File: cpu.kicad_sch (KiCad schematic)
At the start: 22 parts, among them IC1 68HC000, IC2 LHP6323, IC7 MSM54C864

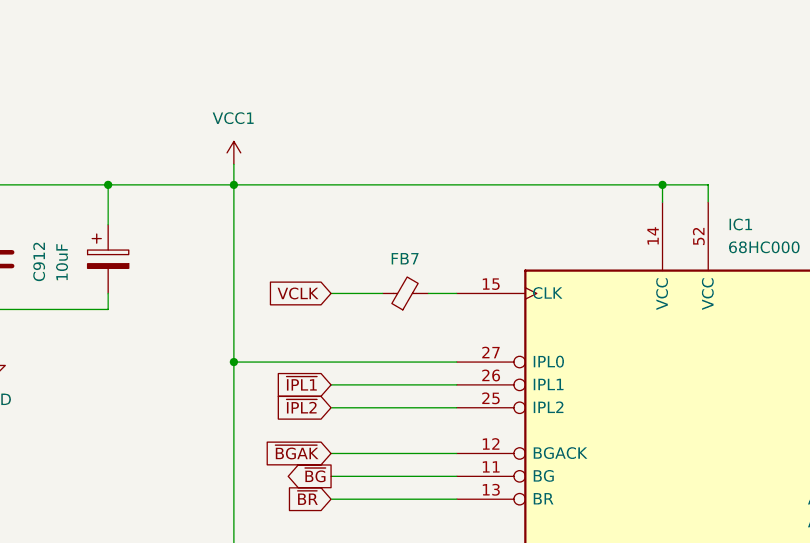
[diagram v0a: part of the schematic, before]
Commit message: Ferrite Bead LCSC Part update
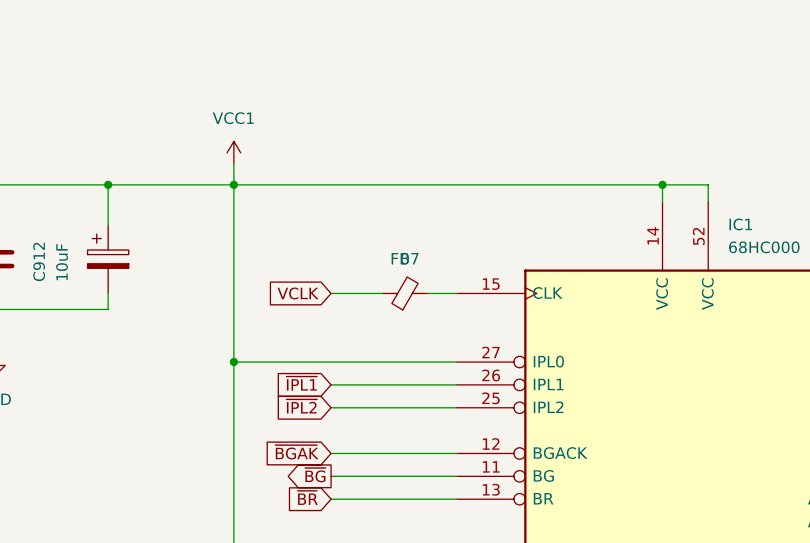
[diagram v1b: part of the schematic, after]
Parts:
- FB7: value ~ -> 0; LCSC Part # C2441367 -> C91037
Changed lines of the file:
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@@
       (effects (font (size 1.27 1.27)))
     )
-    (property "Value" "~" (at 135.2169 55.88 90)
+    (property "Value" "0" (at 135.2169 55.88 90)
       (effects (font (size 1.27 1.27)))
     )
@@
       (effects (font (size 1.27 1.27)) hide)
     )
-    (property "LCSC Part #" "C2441367" (at 135.255 59.69 0)
+    (property "LCSC Part #" "C91037" (at 135.255 59.69 0)
       (effects (font (size 1.27 1.27)) hide)
     )

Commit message: more component parts updated
Full in the * as PAL versions.
Added MPN for PCBWAY
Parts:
- C16, C18, C3, C5: MPN (none) -> VJ0805A101FXJPW1BC
- C17, C2: MPN (none) -> VJ0805A330FXJPW1BC
- C903: MPN (none) -> VJ0805Y223JXJPW1BC
- C903: MPN (none) -> VJ0805Y104JXJMT
- CA601, CA602, CA603, CA604: MPN (none) -> CA0612KRNPO9BN330
- FB7: MPN (none) -> CBG201209U000T
- R3: MPN (none) -> CRCW0805220RFKEAC
- R3: MPN (none) -> CRCW0805150RFKEAHP
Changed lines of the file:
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@@
+      (effects (font (size 1.27 1.27)) hide)
+    )
+    (property "MPN" "CA0612KRNPO9BN330" (at 140.97 231.14 0)
       (effects (font (size 1.27 1.27)) hide)
     )
@@
       (effects (font (size 1.27 1.27)) hide)
     )
+    (property "MPN" "VJ0805Y223JXJPW1BC" (at 323.85 156.21 0)
+      (effects (font (size 1.27 1.27)) hide)
+    )
     (pin "1")
     (pin "2")
@@
     )
     (property "LCSC Part #" "" (at 166.37 115.57 0)
+      (effects (font (size 1.27 1.27)) hide)
+    )
+    (property "MPN" "" (at 166.37 115.57 0)
       (effects (font (size 1.27 1.27)) hide)
     )
@@
       (effects (font (size 1.27 1.27)) hide)
     )
+    (property "MPN" "VJ0805A330FXJPW1BC" (at 65.405 231.14 0)
+      (effects (font (size 1.27 1.27)) hide)
+    )
     (pin "1")
     (pin "2")
@@
     )
     (property "LCSC Part #" "" (at 301.625 193.675 0)
+      (effects (font (size 1.27 1.27)) hide)
+    )
+    (property "MPN" "" (at 301.625 193.675 0)
       (effects (font (size 1.27 1.27)) hide)
     )
@@
       (effects (font (size 1.27 1.27)) hide)
     )
+    (property "MPN" "VJ0805A330FXJPW1BC" (at 349.885 216.535 0)
+      (effects (font (size 1.27 1.27)) hide)
+    )
     (pin "1")
     (pin "2")
@@
       (effects (font (size 1.27 1.27)) hide)
     )
+    (property "MPN" "CRCW0805220RFKEAC" (at 196.85 163.83 0)
+      (effects (font (size 1.27 1.27)) hide)
+    )
     (pin "1")
     (pin "2")
@@
     )
     (property "LCSC Part #" "" (at 333.375 216.535 0)
+      (effects (font (size 1.27 1.27)) hide)
+    )
+    (property "MPN" "" (at 333.375 216.535 0)
       (effects (font (size 1.27 1.27)) hide)
     )
@@
     )
     (property "LCSC Part #" "C576634" (at 102.87 231.14 0)
+      (effects (font (size 1.27 1.27)) hide)
+    )
+    (property "MPN" "CA0612KRNPO9BN330" (at 102.87 231.14 0)
       (effects (font (size 1.27 1.27)) hide)
     )
@@
       (effects (font (size 1.27 1.27)) hide)
     )
+    (property "MPN" "CRCW0805150RFKEAHP" (at 135.255 133.35 0)
+      (effects (font (size 1.27 1.27)) hide)
+    )
     (pin "1")
     (pin "2")
@@
       (effects (font (size 1.27 1.27)) hide)
     )
+    (property "MPN" "VJ0805A101FXJPW1BC" (at 358.14 216.535 0)
+      (effects (font (size 1.27 1.27)) hide)
+    )
     (pin "1")
     (pin "2")
@@
     )
     (property "LCSC Part #" "C2224419" (at 295.91 60.96 0)
+      (effects (font (size 1.27 1.27)) hide)
+    )
+    (property "MPN" "VJ0805Y223JXJPW1BC" (at 295.91 60.96 0)
       (effects (font (size 1.27 1.27)) hide)
     )
@@
       (effects (font (size 1.27 1.27)) hide)
     )
+    (property "MPN" "VJ0805A101FXJPW1BC" (at 341.63 216.535 0)
+      (effects (font (size 1.27 1.27)) hide)
+    )
     (pin "1")
     (pin "2")
@@
     )
     (property "LCSC Part #" "C576634" (at 120.65 231.14 0)
+      (effects (font (size 1.27 1.27)) hide)
+    )
+    (property "MPN" "CA0612KRNPO9BN330" (at 120.65 231.14 0)
       (effects (font (size 1.27 1.27)) hide)
     )
@@
       (effects (font (size 1.27 1.27)) hide)
     )
+    (property "MPN" "VJ0805A101FXJPW1BC" (at 271.145 111.76 0)
+      (effects (font (size 1.27 1.27)) hide)
+    )
     (pin "1")
     (pin "2")
@@
     )
     (property "LCSC Part #" "C576634" (at 163.195 231.14 0)
+      (effects (font (size 1.27 1.27)) hide)
+    )
+    (property "MPN" "CA0612KRNPO9BN330" (at 163.195 231.14 0)
       (effects (font (size 1.27 1.27)) hide)
     )
@@
       (effects (font (size 1.27 1.27)) hide)
     )
+    (property "MPN" "VJ0805A101FXJPW1BC" (at 285.115 111.76 0)
+      (effects (font (size 1.27 1.27)) hide)
+    )
     (pin "1")
     (pin "2")
@@
     )
     (property "LCSC Part #" "" (at 249.555 76.835 0)
+      (effects (font (size 1.27 1.27)) hide)
+    )
+    (property "MPN" "" (at 249.555 76.835 0)
       (effects (font (size 1.27 1.27)) hide)
     )
@@
       (effects (font (size 1.27 1.27)) hide)
     )
+    (property "MPN" "CBG201209U000T" (at 135.255 59.69 0)
+      (effects (font (size 1.27 1.27)) hide)
+    )
     (pin "1")
     (pin "2")
@@
       (effects (font (size 1.27 1.27)) hide)
     )
+    (property "MPN" "" (at 102.235 55.88 0)
+      (effects (font (size 1.27 1.27)) hide)
+    )
     (pin "1")
     (pin "2")
@@
       (effects (font (size 1.27 1.27)) hide)
     )
+    (property "MPN" "VJ0805Y104JXJMT" (at 311.15 156.21 0)
+      (effects (font (size 1.27 1.27)) hide)
+    )
     (pin "1")
     (pin "2")
@@
       (effects (font (size 1.27 1.27)) hide)
     )
+    (property "MPN" "VJ0805Y223JXJPW1BC" (at 89.535 55.88 0)
+      (effects (font (size 1.27 1.27)) hide)
+    )

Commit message: Update LCSC parts
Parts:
- C16, C18, C3, C5: LCSC Part # C2232364 -> C1854109
- C17, C2: LCSC Part # C2232461 -> C520060
- C903: LCSC Part # C2224419 -> C520037
- C903: LCSC Part # C2237864 -> C111492
- R3: LCSC Part # C313835 -> C96210
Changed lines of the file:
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@@
       (effects (font (size 1.27 1.27)) hide)
     )
-    (property "LCSC Part #" "C2224419" (at 323.85 156.21 0)
+    (property "LCSC Part #" "C520037" (at 323.85 156.21 0)
       (effects (font (size 1.27 1.27)) hide)
     )
@@
       (effects (font (size 1.27 1.27)) hide)
     )
-    (property "LCSC Part #" "C2232461" (at 65.405 231.14 0)
+    (property "LCSC Part #" "C520060" (at 65.405 231.14 0)
       (effects (font (size 1.27 1.27)) hide)
     )
@@
       (effects (font (size 1.27 1.27)) hide)
     )
-    (property "LCSC Part #" "C2232461" (at 349.885 216.535 0)
+    (property "LCSC Part #" "C520060" (at 349.885 216.535 0)
       (effects (font (size 1.27 1.27)) hide)
     )
@@
       (effects (font (size 1.27 1.27)) hide)
     )
-    (property "LCSC Part #" "C313835" (at 135.255 133.35 0)
+    (property "LCSC Part #" "C96210" (at 135.255 133.35 0)
       (effects (font (size 1.27 1.27)) hide)
     )
@@
       (effects (font (size 1.27 1.27)) hide)
     )
-    (property "LCSC Part #" "C2232364" (at 358.14 216.535 0)
+    (property "LCSC Part #" "C1854109" (at 358.14 216.535 0)
       (effects (font (size 1.27 1.27)) hide)
     )
@@
       (effects (font (size 1.27 1.27)) hide)
     )
-    (property "LCSC Part #" "C2224419" (at 295.91 60.96 0)
+    (property "LCSC Part #" "C520037" (at 295.91 60.96 0)
       (effects (font (size 1.27 1.27)) hide)
     )
@@
       (effects (font (size 1.27 1.27)) hide)
     )
-    (property "LCSC Part #" "C2232364" (at 341.63 216.535 0)
+    (property "LCSC Part #" "C1854109" (at 341.63 216.535 0)
       (effects (font (size 1.27 1.27)) hide)
     )
@@
       (effects (font (size 1.27 1.27)) hide)
     )
-    (property "LCSC Part #" "C2232364" (at 271.145 111.76 0)
+    (property "LCSC Part #" "C1854109" (at 271.145 111.76 0)
       (effects (font (size 1.27 1.27)) hide)
     )
@@
       (effects (font (size 1.27 1.27)) hide)
     )
-    (property "LCSC Part #" "C2232364" (at 285.115 111.76 0)
+    (property "LCSC Part #" "C1854109" (at 285.115 111.76 0)
       (effects (font (size 1.27 1.27)) hide)
     )
@@
       (effects (font (size 1.27 1.27)) hide)
     )
-    (property "LCSC Part #" "C2237864" (at 311.15 156.21 0)
+    (property "LCSC Part #" "C111492" (at 311.15 156.21 0)
       (effects (font (size 1.27 1.27)) hide)
     )
@@
       (effects (font (size 1.27 1.27)) hide)
     )
-    (property "LCSC Part #" "C2224419" (at 89.535 55.88 0)
-      (effects (font (size 1.27 1.27)) hide)
-    )
+    (property "LCSC Part #" "C520037" (at 89.535 55.88 0)
+      (effects (font (size 1.27 1.27)) hide)
+    )

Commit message: Longer pads for IC1.
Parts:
- IC1: footprint Package_LCC:PLCC-68 -> Neptune:PLCC-68
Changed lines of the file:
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@@
       (effects (font (size 1.27 1.27)) (justify left))
     )
-    (property "Footprint" "Package_LCC:PLCC-68" (at 147.32 58.42 0)
+    (property "Footprint" "Neptune:PLCC-68" (at 147.32 58.42 0)
       (effects (font (size 1.27 1.27)) hide)
     )

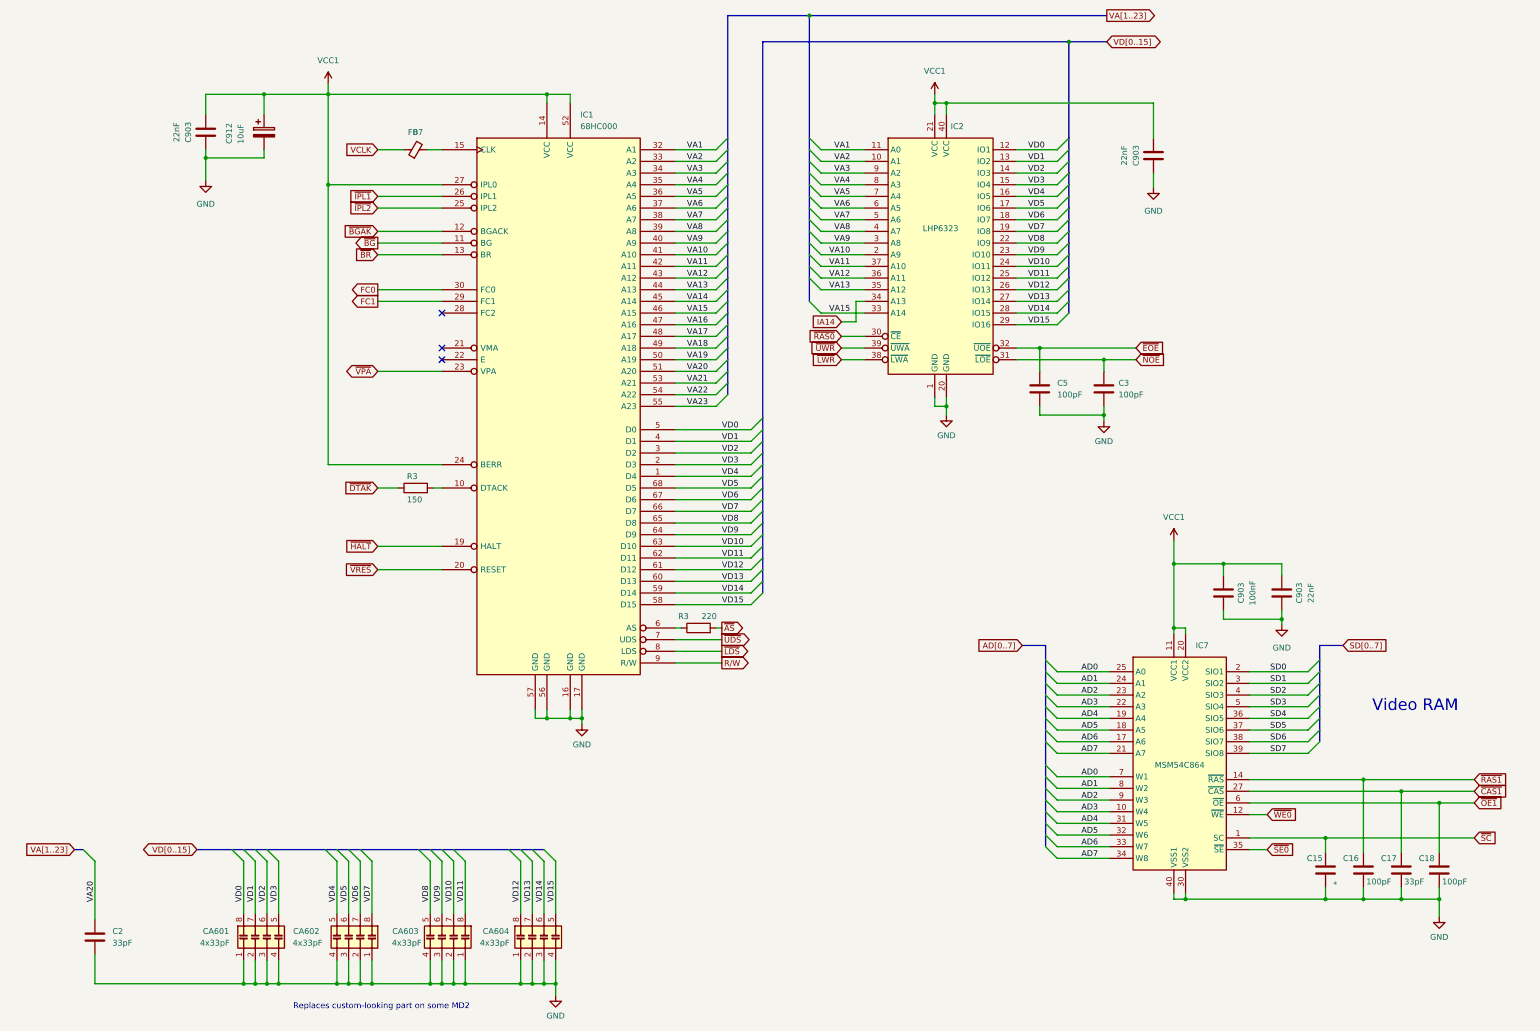
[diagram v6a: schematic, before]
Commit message: MRES diode fix, use more common BGKR LED pinout and larger footprint.
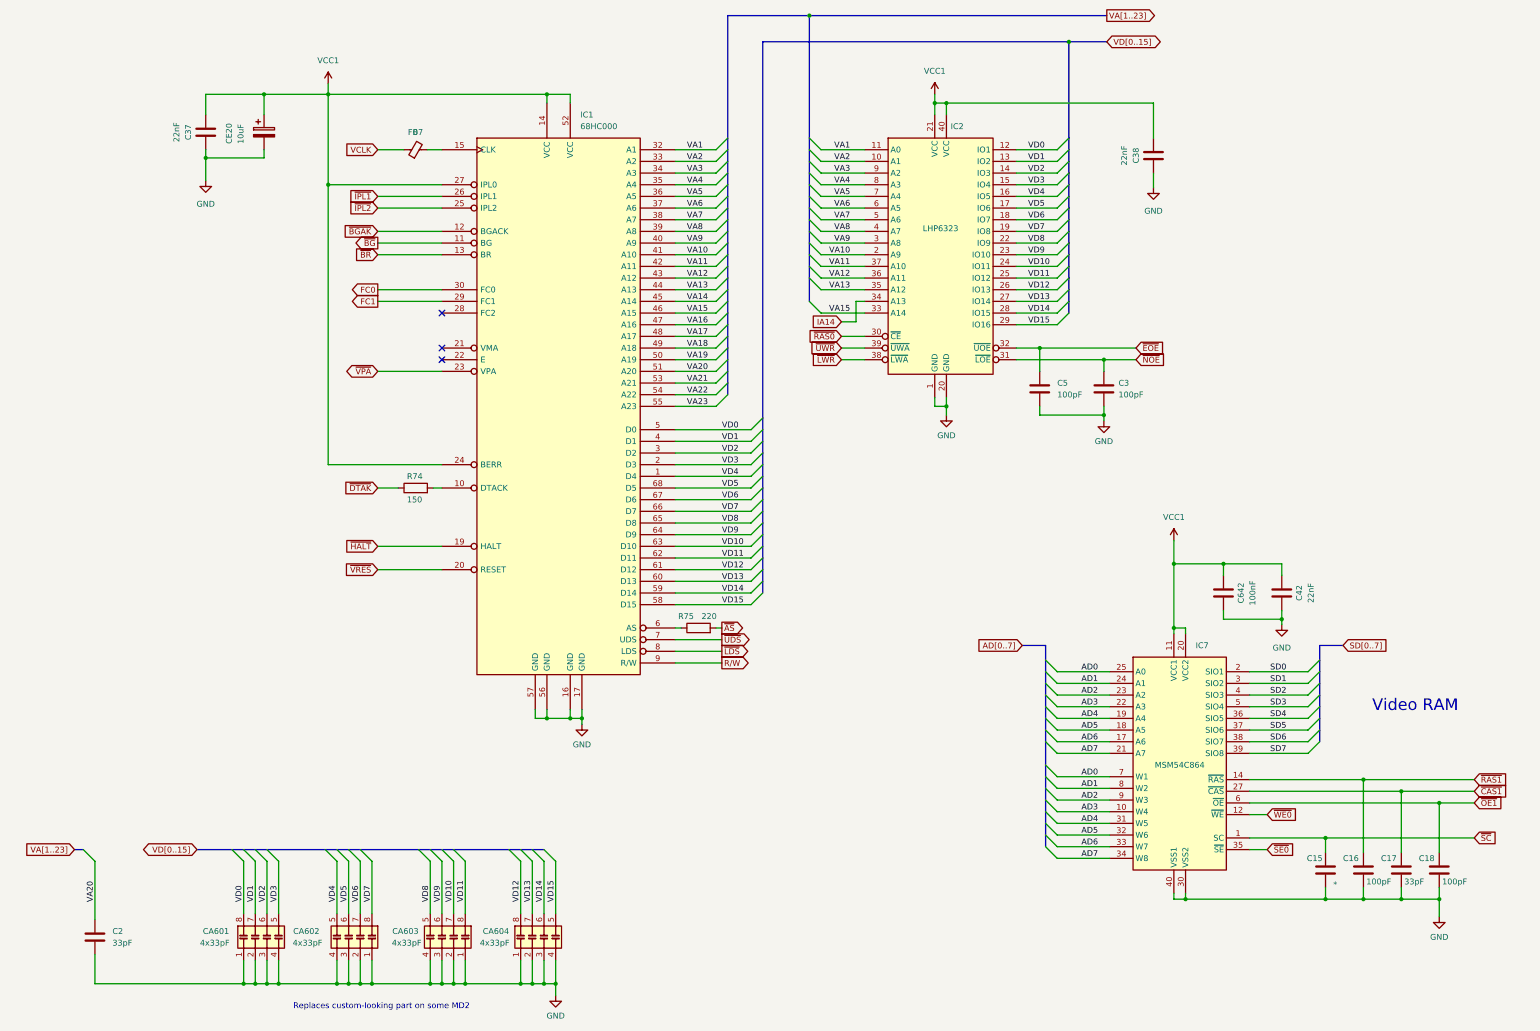
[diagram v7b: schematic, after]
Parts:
- renumbered C903 to C37, C903 to C38, C903 to C42, C903 to C642, C912 to CE20, R3 to R74, R3 to R75
